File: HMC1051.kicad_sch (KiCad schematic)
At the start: 43 parts, among them U1 LMV324

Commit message: MCU interfaces are done! Check the Changes and Complete ERC modifications
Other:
- company: (none) -> Parikshit Student Satellite Team
- title: (none) -> AOCS BOARD
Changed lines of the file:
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@@
 (kicad_sch (version 20211123) (generator eeschema)
   (paper "A4")
+  (title_block
+    (title "AOCS BOARD")
+    (company "Parikshit Student Satellite Team")
+  )
   (junction (at 147.32 66.04) (diameter 0) (color 0 0 0 0)
   )
@@
   )
   (wire (pts (xy 71.12 154.94) (xy 71.12 163.83))
+    (stroke (width 0) (type default) (color 0 0 0 0))
+  )
+  (wire (pts (xy 276.225 153.67) (xy 276.225 152.4))
     (stroke (width 0) (type default) (color 0 0 0 0))
   )
@@
     (pin "1")
   )
+  (symbol (lib_id "power:PWR_FLAG") (at 276.225 152.4 0) (unit 1)
+    (in_bom yes) (on_board yes) (fields_autoplaced)
+    (property "Reference" "#FLG0102" (id 0) (at 276.225 150.495 0)
+      (effects (font (size 1.27 1.27)) hide)
+    )
+    (property "Value" "PWR_FLAG" (id 1) (at 276.225 146.685 0))
+    (property "Footprint" "" (id 2) (at 276.225 152.4 0)
+      (effects (font (size 1.27 1.27)) hide)
+    )
+    (property "Datasheet" "~" (id 3) (at 276.225 152.4 0)
+      (effects (font (size 1.27 1.27)) hide)
+    )
+    (pin "1")
+  )
   (symbol (lib_id "Device:R") (at 25.4 100.33 0) (unit 1)
     (in_bom yes) (on_board yes) (fields_autoplaced)
@@
     (pin "2")
   )
+  (symbol (lib_id "power:GND") (at 276.225 153.67 0) (unit 1)
+    (in_bom yes) (on_board yes) (fields_autoplaced)
+    (property "Reference" "#PWR0266" (id 0) (at 276.225 160.02 0)
+      (effects (font (size 1.27 1.27)) hide)
+    )
+    (property "Value" "GND" (id 1) (at 276.225 158.115 0))
+    (property "Footprint" "" (id 2) (at 276.225 153.67 0)
+      (effects (font (size 1.27 1.27)) hide)
+    )
+    (property "Datasheet" "" (id 3) (at 276.225 153.67 0)
+      (effects (font (size 1.27 1.27)) hide)
+    )
+    (pin "1")
+  )
   (symbol (lib_id "Device:R") (at 49.53 139.7 180) (unit 1)

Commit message: added notes
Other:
- note added: "FERRITE YET TBD"
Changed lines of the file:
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@@
     (effects (font (size 1.27 1.27)) (justify left bottom))
+  )
+  (text "FERRITE YET TBD" (at 167.64 143.51 0)
+    (effects (font (size 2.54 2.54) (thickness 0.508) bold) (justify left bottom))
   )
   (text "before finalising capacitors \nsimulate the PDN on SPICE to ensure \nthere isnt any ringing because of unintentional \ntank formation\n"

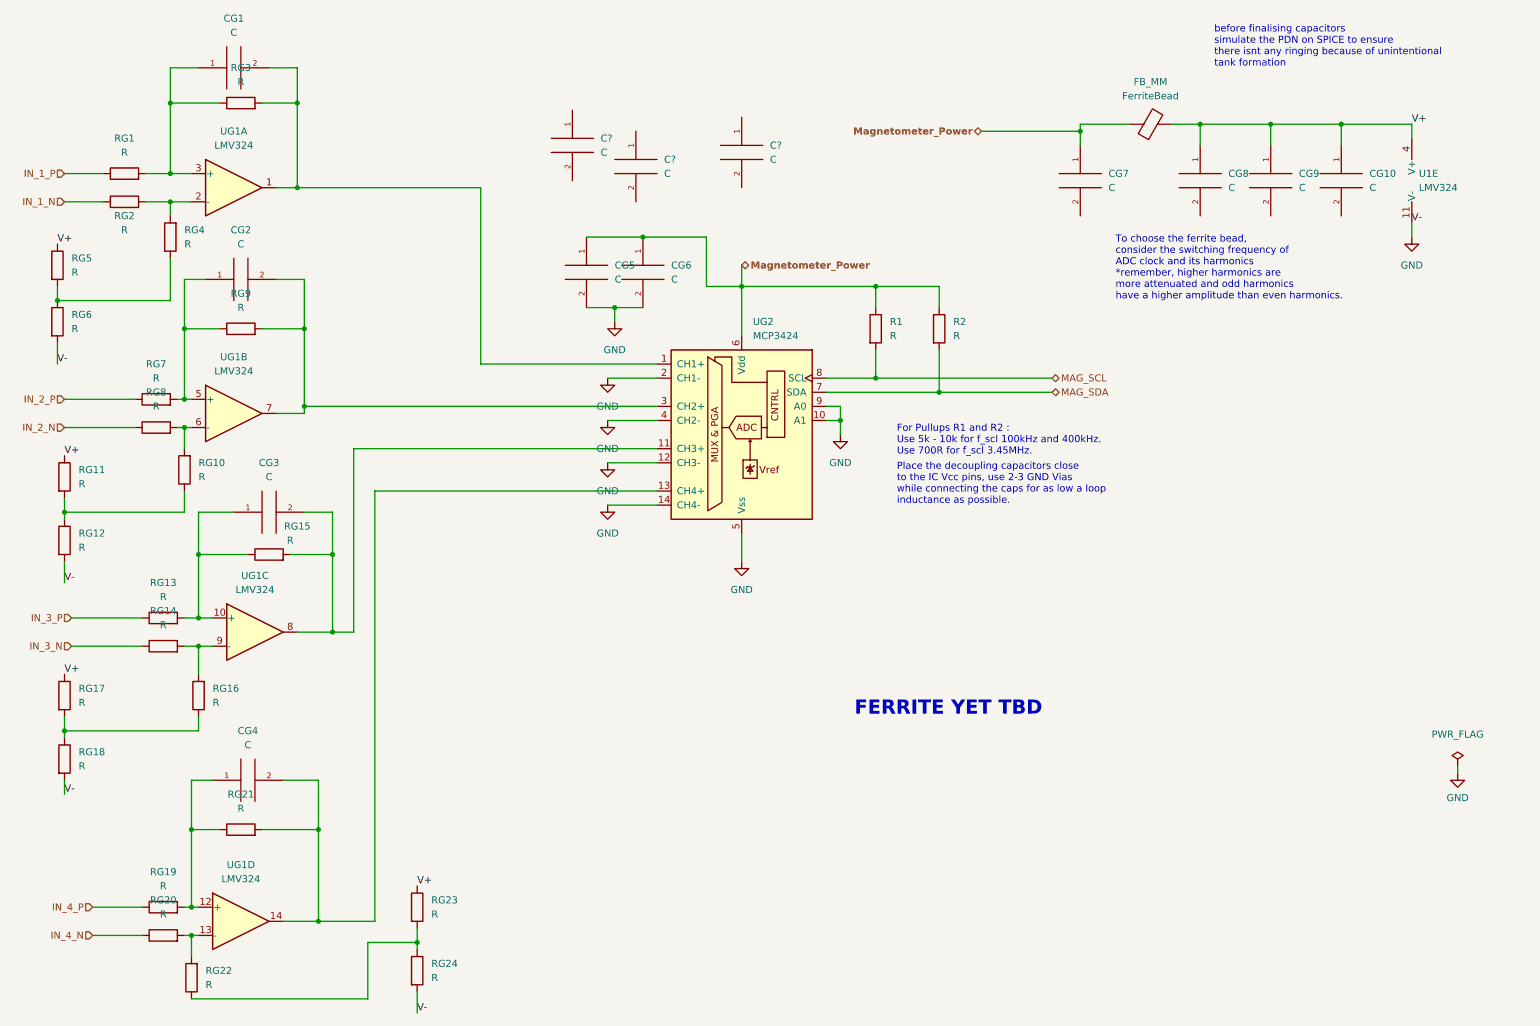
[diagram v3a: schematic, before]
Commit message: Max ERC errors corrected
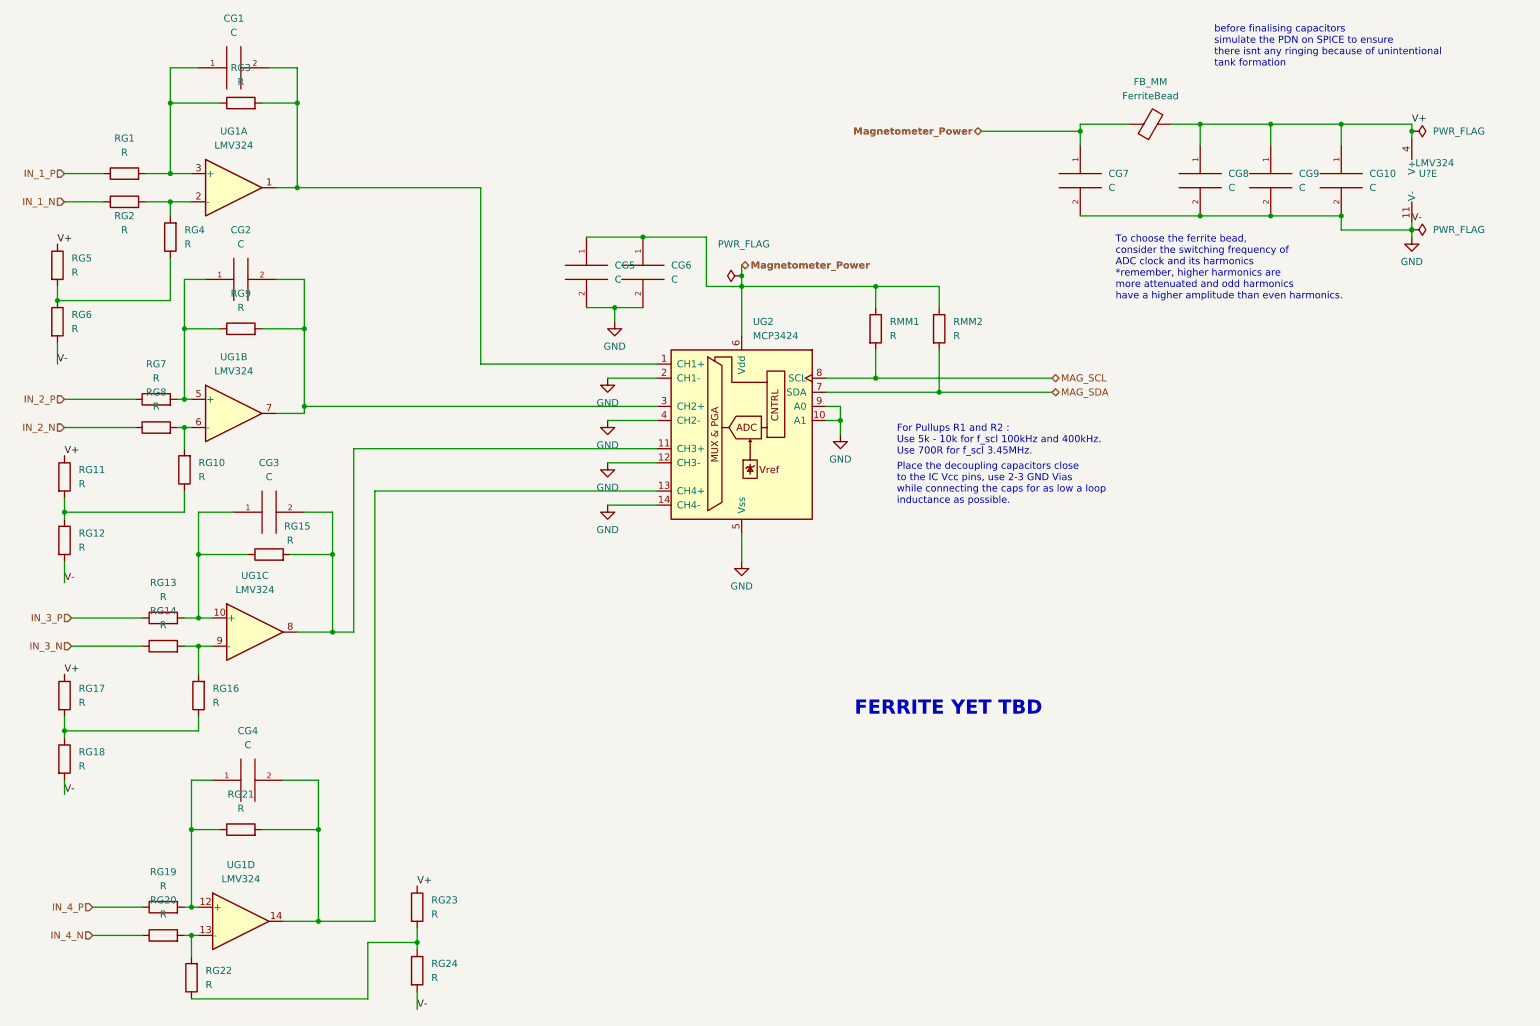
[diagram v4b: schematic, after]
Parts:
- removed C? (x3): C, symbol pspice:C
- renumbered R1 to RMM1, R2 to RMM2, U1 to U?
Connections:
- net GND: now also CG10.2, CG7.2, CG8.2, CG9.2

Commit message: Updated the changes
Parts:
- gave numbers to parts that had none: 1
- renumbered CG4 to CG10, CG7 to CG2, CG8 to CG3, CG9 to CG4, CG10 to CG5, CG5 to CG6, CG6 to CG7, CG2 to CG8, CG3 to CG9, FB_MM to FB_MM1, RG3 to RG1, RG15 to RG13, RG13 to RG14, RG14 to RG15, RG17 to RG16, RG16 to RG17, RG21 to RG19, RG1 to RG2, RG19 to RG20, RG23 to RG21, RG20 to RG22, RG24 to RG23, RG22 to RG24, RG2 to RG3, RG9 to RG7, RG7 to RG8, RG8 to RG9
